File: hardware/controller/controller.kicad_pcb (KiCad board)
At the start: 2 copper layers, 48 x 88.5 mm, 19 parts, among them J1 Conn_01x02_Pin, J2 Conn_01x02_Pin, J3 Conn_01x02_Pin, J4 Conn_01x02_Pin

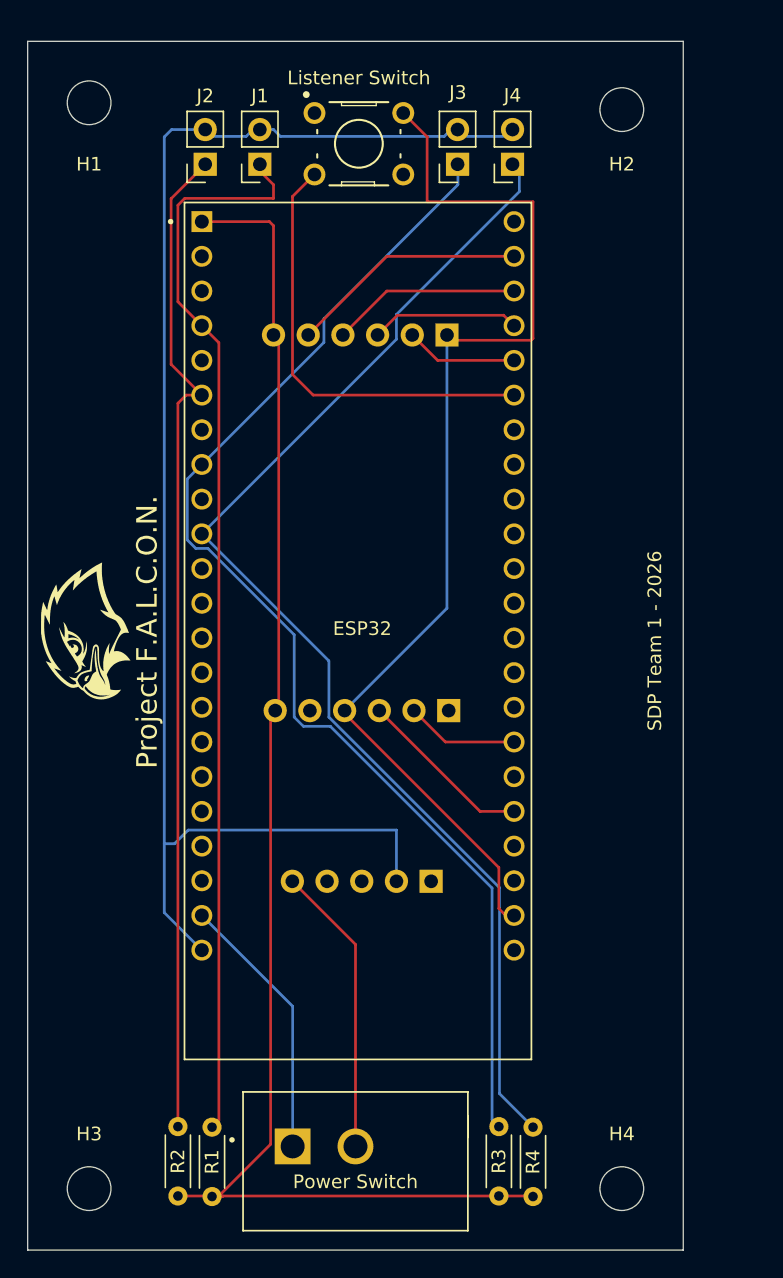
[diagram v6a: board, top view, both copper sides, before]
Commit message: redesign of part placements on PCB, measurement confirmed
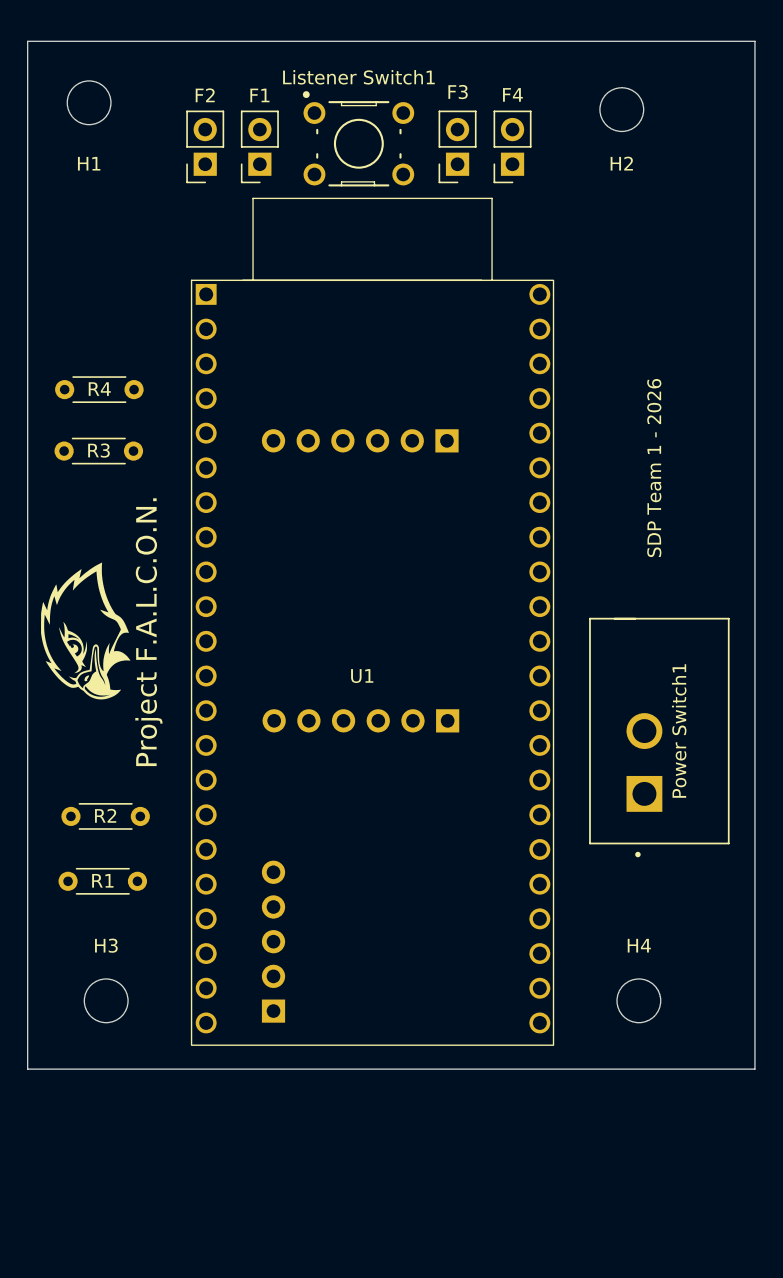
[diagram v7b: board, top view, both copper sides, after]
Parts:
- removed ESP32: ESP32-S3-DEVKITC-1-N8R8, ESP32-S3-DEVKITC-1-N8R8:ESP32-S3-DEVKITC-1-N8R8
- added U1: ESP32-S3-DEVKITC-1-N8R8, SANXIXING ESP32-S3:ESP32-S3-DEVKITC-1-N8R8, F.Cu at (139.0, 102.0)
- Listener Switch1: renamed from Listener Switch
- Power Switch1: renamed from Power Switch
- moved R4 64.0 mm to (117.2, 79.0), turned to 0 degrees
- moved R3 60.7 mm to (122.2, 83.5), turned to 180 degrees
- moved Power Switch1 38.6 mm to (160.8, 104.0), turned to 90 degrees
- moved R2 24.0 mm to (117.7, 110.2), turned to 0 degrees
- moved R1 20.9 mm to (117.5, 115.0), turned to 0 degrees
- moved USB C Lipo1 14.9 mm to (132.5, 124.5), turned to 0 degrees
- moved H3 13.8 mm to (120.2, 123.8)
- moved H4 13.8 mm to (159.2, 123.8)
- moved UWB1 7.75 mm to (145.2, 82.8)
- moved IMU1 0.75 mm to (145.2, 103.2)
- renumbered J1 to F1, J2 to F2, J3 to F3, J4 to F4
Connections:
- IMU1 pad 4: Net-(ESP32-GND1) -> Net-(IMU1-Pin_4)
- IMU1 pad 6: Net-(ESP32-3V3) -> Net-(IMU1-Pin_6)
- Listener Switch1 pad 2: Net-(ESP32-GND1) -> Net-(IMU1-Pin_6)
- Power Switch1 pad 2: Net-(USB C Lipo1-Pin_5) -> Net-(USB C Lipo1-Pin_1)
- R1 pad 2: Net-(ESP32-3V3) -> Net-(IMU1-Pin_6)
- R2 pad 2: Net-(ESP32-3V3) -> Net-(IMU1-Pin_6)
- R3 pad 1: Net-(ESP32-3V3) -> Net-(IMU1-Pin_6)
- R4 pad 2: Net-(ESP32-3V3) -> Net-(IMU1-Pin_6)
- USB C Lipo1 pad 1: unconnected-(USB C Lipo1-Pin_1-Pad1) -> Net-(USB C Lipo1-Pin_1)
- USB C Lipo1 pad 5: Net-(USB C Lipo1-Pin_5) -> unconnected-(USB C Lipo1-Pin_5-Pad5)
- UWB1 pad 1: Net-(ESP32-GND1) -> Net-(IMU1-Pin_4)
- UWB1 pad 2: Net-(ESP32-GPIO2) -> unconnected-(UWB1-Pin_2-Pad2)
- UWB1 pad 5: Net-(ESP32-U0TXD/GPIO43) -> unconnected-(UWB1-Pin_5-Pad5)
- UWB1 pad 6: Net-(ESP32-3V3) -> Net-(IMU1-Pin_6)
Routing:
- net Net-(F1-Pin_2): track 108.8 -> 0.00 mm
- net Net-(ESP32-3V3): track 104.8 -> 0.00 mm
- net Net-(F4-Pin_1): track 90.4 -> 0.00 mm
- net Net-(F3-Pin_1): track 90.0 -> 0.00 mm
- net Net-(ESP32-GND1): track 82.6 -> 0.00 mm
- net Net-(F1-Pin_1): track 79.1 -> 0.00 mm
- net Net-(F2-Pin_1): track 73.8 -> 0.00 mm
- net Net-(U1-GPIO18): track 32.2 -> 0.00 mm
- net Net-(USB C Lipo1-Pin_5): track 20.9 -> 0.00 mm
- net Net-(U1-5V0): track 19.3 -> 0.00 mm
- net Net-(ESP32-U0TXD/GPIO43): track 17.5 -> 0.00 mm
- net Net-(U1-U0TXD/GPIO43): track 13.9 -> 0.00 mm
- net Net-(IMU1-Pin_3): track 12.9 -> 0.00 mm
- net Net-(U1-U0RXD/GPIO44): track 10.9 -> 0.00 mm
- net Net-(IMU1-Pin_2): track 8.28 -> 0.00 mm
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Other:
- board size 48 x 88.5 mm -> 53.2 x 75.2 mm

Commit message: PCB routing done
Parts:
- moved R1 41.5 mm to (117.8, 73.5)
- moved R2 41.5 mm to (117.8, 68.8)
- moved R4 40.8 mm to (156.8, 69.0)
- moved R3 40.7 mm to (161.8, 73.5)
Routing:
- net Net-(F1-Pin_2): track 0.00 -> 106.8 mm
- net Net-(IMU1-Pin_6): track 0.00 -> 94.4 mm
- net Net-(F4-Pin_1): track 0.00 -> 52.7 mm
- net Net-(F3-Pin_1): track 0.00 -> 51.0 mm
- net Net-(U1-5V0): track 0.00 -> 49.3 mm
- net Net-(IMU1-Pin_4): track 0.00 -> 49.2 mm
- net Net-(U1-GPIO18): track 0.00 -> 41.0 mm
- net Net-(USB C Lipo1-Pin_1): track 0.00 -> 35.7 mm
- net Net-(F2-Pin_1): track 0.00 -> 33.8 mm
- net Net-(F1-Pin_1): track 0.00 -> 32.4 mm
- net Net-(IMU1-Pin_3): track 0.00 -> 18.1 mm
- net Net-(U1-U0TXD/GPIO43): track 0.00 -> 17.8 mm
- net Net-(U1-U0RXD/GPIO44): track 0.00 -> 14.2 mm
- net Net-(IMU1-Pin_2): track 0.00 -> 12.8 mm
